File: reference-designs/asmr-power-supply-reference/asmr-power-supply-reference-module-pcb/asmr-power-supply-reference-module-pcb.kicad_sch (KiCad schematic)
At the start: 2 parts

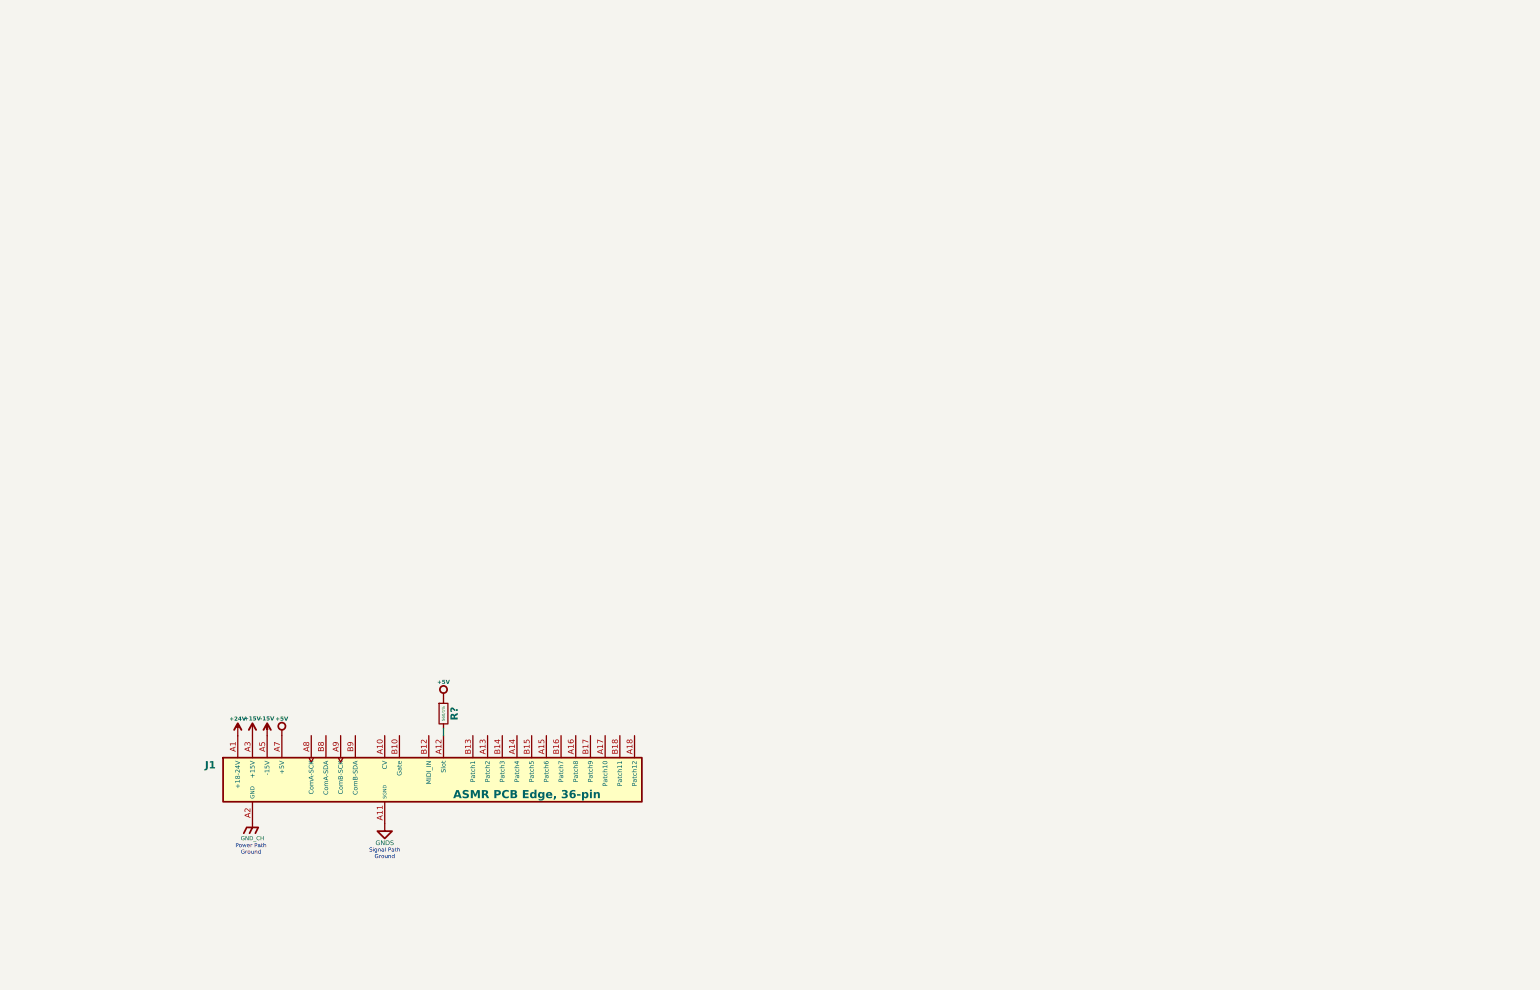
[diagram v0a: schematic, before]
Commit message: First pass on the power supply module.
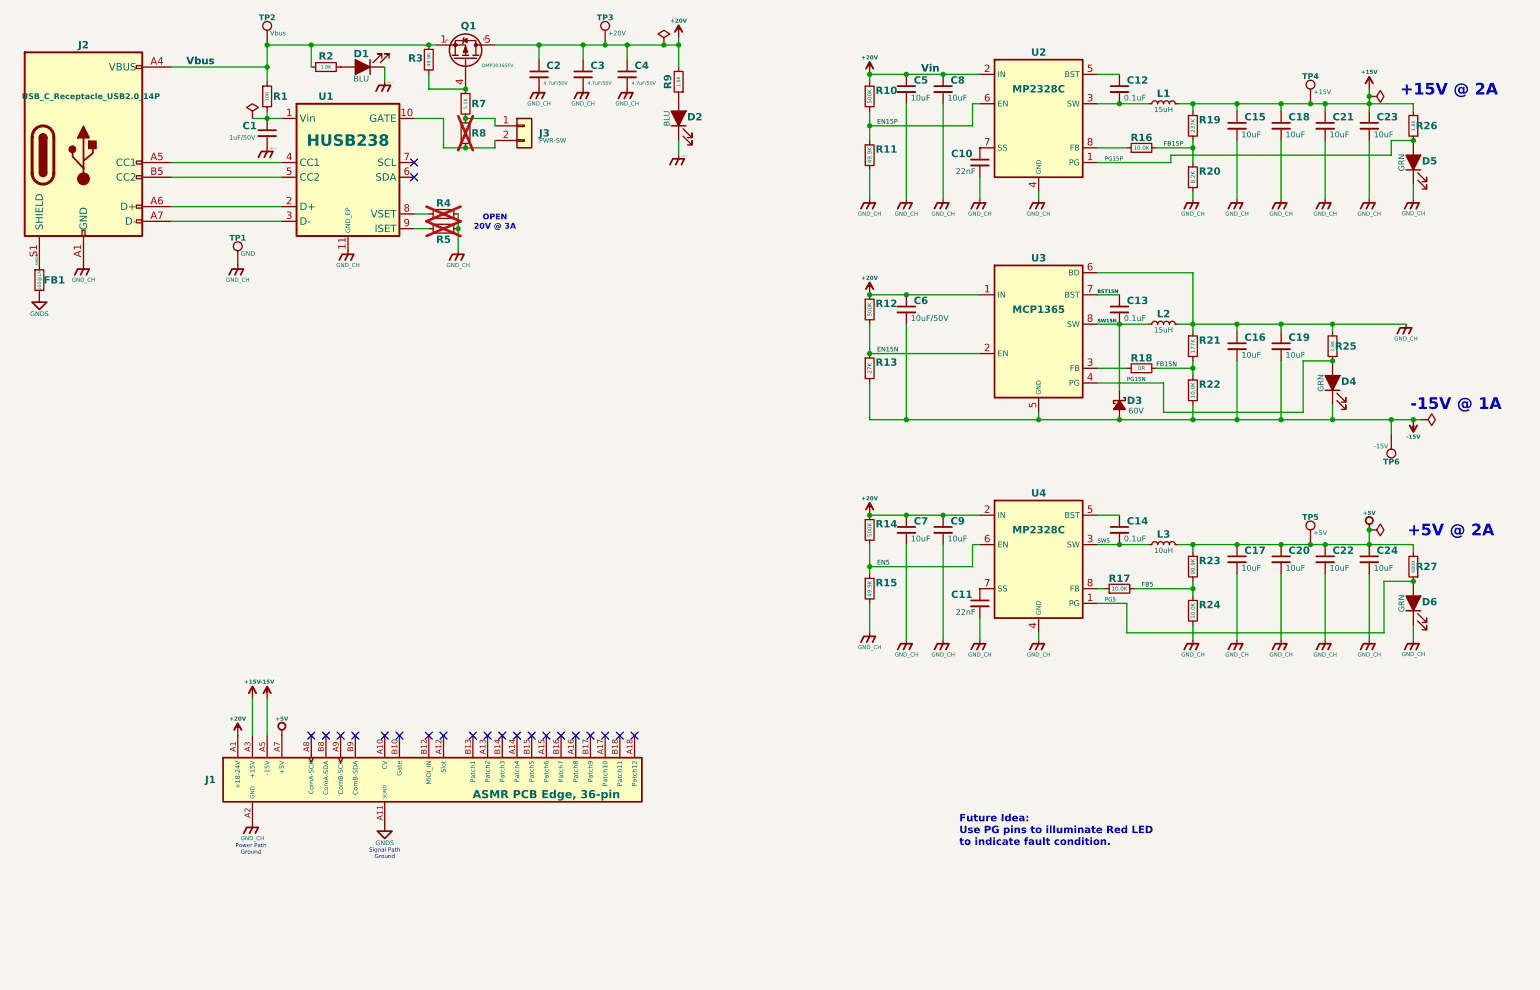
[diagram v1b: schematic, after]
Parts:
- removed R?: 560/1%, symbol CM_Device:R
- added C1: 1uF/50V, CM_Resistor_Capacitor:C_0603_1608Metric, symbol Device:C_Small
- added C10, C11: 22nF, CM_Resistor_Capacitor:C_0603_1608Metric, symbol Device:C_Small
- added C12, C13, C14: 0.1uF, CM_Resistor_Capacitor:C_0603_1608Metric, symbol Device:C_Small
- added C15, C16, C17, C18, C19, C20, C21, C22, C23, C24, C5, C7, C8, C9: 10uF, Capacitor_SMD:C_1206_3216Metric, symbol Device:C_Small
- added C2, C3, C4: 4.7uF/50V, CM_Resistor_Capacitor:C_0603_1608Metric, symbol Device:C_Small
- added C6: 10uF/50V, Capacitor_SMD:C_1206_3216Metric, symbol Device:C_Small
- added D1, D2: BLU, LED_SMD:LED_0603_1608Metric, symbol Device:LED_Filled
- added D3: 60V, Diode_SMD:D_SMF, symbol Device:D_Schottky_Small_Filled
- added D4, D5, D6: GRN, LED_SMD:LED_0603_1608Metric, symbol Device:LED_Filled
- added FB1: 100@1M, CM_Resistor_Capacitor:R_0603_1608Metric, symbol CM_Device:R
- added J2: USB_C_Receptacle_USB2.0_14P, Connector_USB:USB_C_Receptacle_HCTL_HC-TYPE-C-16P-01A, symbol CM_Connector_USB:USB_C_Receptacle_USB2.0_14P
- added J3: PWR-SW, Connector_JST:JST_SH_BM02B-SRSS-TB_1x02-1MP_P1.00mm_Vertical, symbol Connector_Generic:Conn_01x02
- added L1, L2: 15uH, CM_Inductor:SRN5040, symbol Device:L_Small
- added L3: 10uH, CM_Inductor:SRN5040, symbol Device:L_Small
- added Q1: DMP3036SFV, Package_SON:VSON-8_3.3x3.3mm_P0.65mm_NexFET, symbol CM_Transistors_FETs:DMP3036SFV
- added R1: 10R, CM_Resistor_Capacitor:R_0603_1608Metric, symbol CM_Device:R
- added R10, R12, R14: 500K, CM_Resistor_Capacitor:R_0603_1608Metric, symbol Device:R_Small
- added R11, R15: 49.9K, CM_Resistor_Capacitor:R_0603_1608Metric, symbol Device:R_Small
- added R13: 27K, CM_Resistor_Capacitor:R_0603_1608Metric, symbol Device:R_Small
- added R16, R17, R22, R24: 10.0K, CM_Resistor_Capacitor:R_0603_1608Metric, symbol Device:R_Small
- added R18: 0R, CM_Resistor_Capacitor:R_0603_1608Metric, symbol Device:R_Small
- added R19: 237K, CM_Resistor_Capacitor:R_0603_1608Metric, symbol Device:R_Small
- added R2, R25, R26, R9: 1.8K, CM_Resistor_Capacitor:R_0603_1608Metric, symbol CM_Device:R
- added R20: 8.2K, CM_Resistor_Capacitor:R_0603_1608Metric, symbol Device:R_Small
- added R21: 177K, CM_Resistor_Capacitor:R_0603_1608Metric, symbol Device:R_Small
- added R23: 90.9K, CM_Resistor_Capacitor:R_0603_1608Metric, symbol Device:R_Small
- added R27: 680R, CM_Resistor_Capacitor:R_0603_1608Metric, symbol CM_Device:R
- added R3: 49.9K, CM_Resistor_Capacitor:R_0603_1608Metric, symbol CM_Device:R
- added R4, R5: NS, CM_Resistor_Capacitor:R_0603_1608Metric, symbol CM_Device:R
- added R7: 5.1K, CM_Resistor_Capacitor:R_0603_1608Metric, symbol CM_Device:R
- added R8: 0R, CM_Resistor_Capacitor:R_0603_1608Metric, symbol CM_Device:R
- added TP1: GND, TestPoint:TestPoint_Keystone_5015_Micro_Mini, symbol Connector:TestPoint
- added TP2: Vbus, TestPoint:TestPoint_Keystone_5015_Micro_Mini, symbol Connector:TestPoint
- added TP3: +20V, TestPoint:TestPoint_Keystone_5015_Micro_Mini, symbol Connector:TestPoint
- added TP4: +15V, TestPoint:TestPoint_Keystone_5015_Micro_Mini, symbol Connector:TestPoint
- added TP5: +5V, TestPoint:TestPoint_Keystone_5015_Micro_Mini, symbol Connector:TestPoint
- added TP6: -15V, TestPoint:TestPoint_Keystone_5015_Micro_Mini, symbol Connector:TestPoint
- added U1: HUSB238, Package_DFN_QFN:DFN-10-1EP_3x3mm_P0.5mm_EP1.65x2.38mm, symbol CM_Connector_USB:Chip-HUSB238-DFN10
- added U2, U4: MP2328C, Package_TO_SOT_SMD:SOT-583-8, symbol CM_regulator_switching:MP2328C
- added U3: MCP1365, Package_DFN_QFN:DFN-8-1EP_3x3mm_P0.65mm_EP1.55x2.4mm, symbol CM_regulator_switching:MCP1365
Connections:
- net +15V: now also C15.1, C18.1, C21.1, C23.1, L1.2, R19.1, R26.2, TP4.1
- net +5V: now also C17.1, C20.1, C22.1, C24.1, L3.2, R23.1, R27.2, TP5.1
- net -15V: now also C16.2, C19.2, C6.2, D3.2 (A), D4.1 (K), R13.2, R22.2, TP6.1, U3.5 (GND), U3.9 (EP)
- net GNDS: now also FB1.2
- net +24V renamed +18-24V
- net +18-24V: now also C2.1, C3.1, C4.1, C5.1, C6.1, C7.1, C8.1, C9.1, Q1.5 (S), R10.1, R12.1, R14.1, R9.2, TP3.1, U2.2 (IN), U3.1 (IN), U4.2 (IN)
- net GND_CH renamed GND
- net GND: now also C1.2, C10.2, C11.2, C15.2, C16.1, C17.2, C18.2, C19.1, C2.2, C20.2, C21.2, C22.2, C23.2, C24.2, C3.2, C4.2, C5.2, C7.2, C8.2, C9.2, D1.1 (K), D2.1 (K), D5.1 (K), D6.1 (K), J2.A1 (GND), J2.A12 (GND), J2.B1 (GND), J2.B12 (GND), L2.2, R11.2, R15.2, R20.2, R21.1, R24.2, R25.2, R4.2, R5.2, TP1.1, U1.11 (GND_EP), U2.4 (GND), U3.6 (BD), U4.4 (GND)
- new net: J3.1 (Pin_1), R7.2, R8.1
- new net: J3.2 (Pin_2), R8.2, U1.10 (GATE)
- new net: J2.A5 (CC1), U1.4 (CC1)
- new net: J2.A6 (D+), J2.B6 (D+), U1.2 (D+)
- new net: J2.A7 (D-), J2.B7 (D-), U1.3 (D-)
- new net: J2.B5 (CC2), U1.5 (CC2)
- new net: R5.1, U1.9 (ISET)
- new net: R4.1, U1.8 (VSET)
- new net: C10.1, U2.7 (SS)
- new net: D2.2 (A), R9.1
- new net: C12.1, U2.5 (BST)
- new net: C12.2, L1.1, U2.3 (SW)
- new net: R18.1, U3.3 (FB)
- new net: C1.1, R1.2, U1.1 (Vin)
- new net: R16.1, U2.8 (FB)
- new net: C14.1, U4.5 (BST)
- new net: C11.1, U4.7 (SS)
- new net: R17.1, U4.8 (FB)
- new net: D1.2 (A), R2.2
- new net: Q1.4 (G), R3.2, R7.1
- new net BST15N: C13.1, U3.7 (BST)
- new net EN15N: R12.2, R13.1, U3.2 (EN)
- new net EN15P: R10.2, R11.1, U2.6 (EN)
- new net EN5: R14.2, R15.1, U4.6 (EN)
- new net FB15N: R18.2, R21.2, R22.1
- new net FB15P: R16.2, R19.2, R20.1
- new net FB5: R17.2, R23.2, R24.1
- new net PG15N: D4.2 (A), R25.1, U3.4 (PG)
- new net PG15P: D5.2 (A), R26.1, U2.1 (PG)
- new net PG5: D6.2 (A), R27.1, U4.1 (PG)
- new net SHIELD: FB1.1, J2.S1 (SHIELD)
- new net SW15N: C13.2, D3.1 (K), L2.1, U3.8 (SW)
- new net SW5: C14.2, L3.1, U4.3 (SW)
- new net Vbus: J2.A4 (VBUS), J2.A9 (VBUS), J2.B4 (VBUS), J2.B9 (VBUS), Q1.1 (D), Q1.2 (D), Q1.3 (D), R1.1, R2.1, R3.1, TP2.1
- no-connect marks 0 -> 22
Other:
- note added: "+15V @ 2A"
- note added: "+5V @ 2A"
- note added: "-15V @ 1A"
- note added: "Future Idea: Use PG pins to illuminate Red LED to indicate fault condition."
- note added: "OPEN 20V @ 3A"
- title: ASMR - Module PCB Reference Design -> Power Supply Module PCB Reference Design

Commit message: Update design with 64 pin PCI connector.
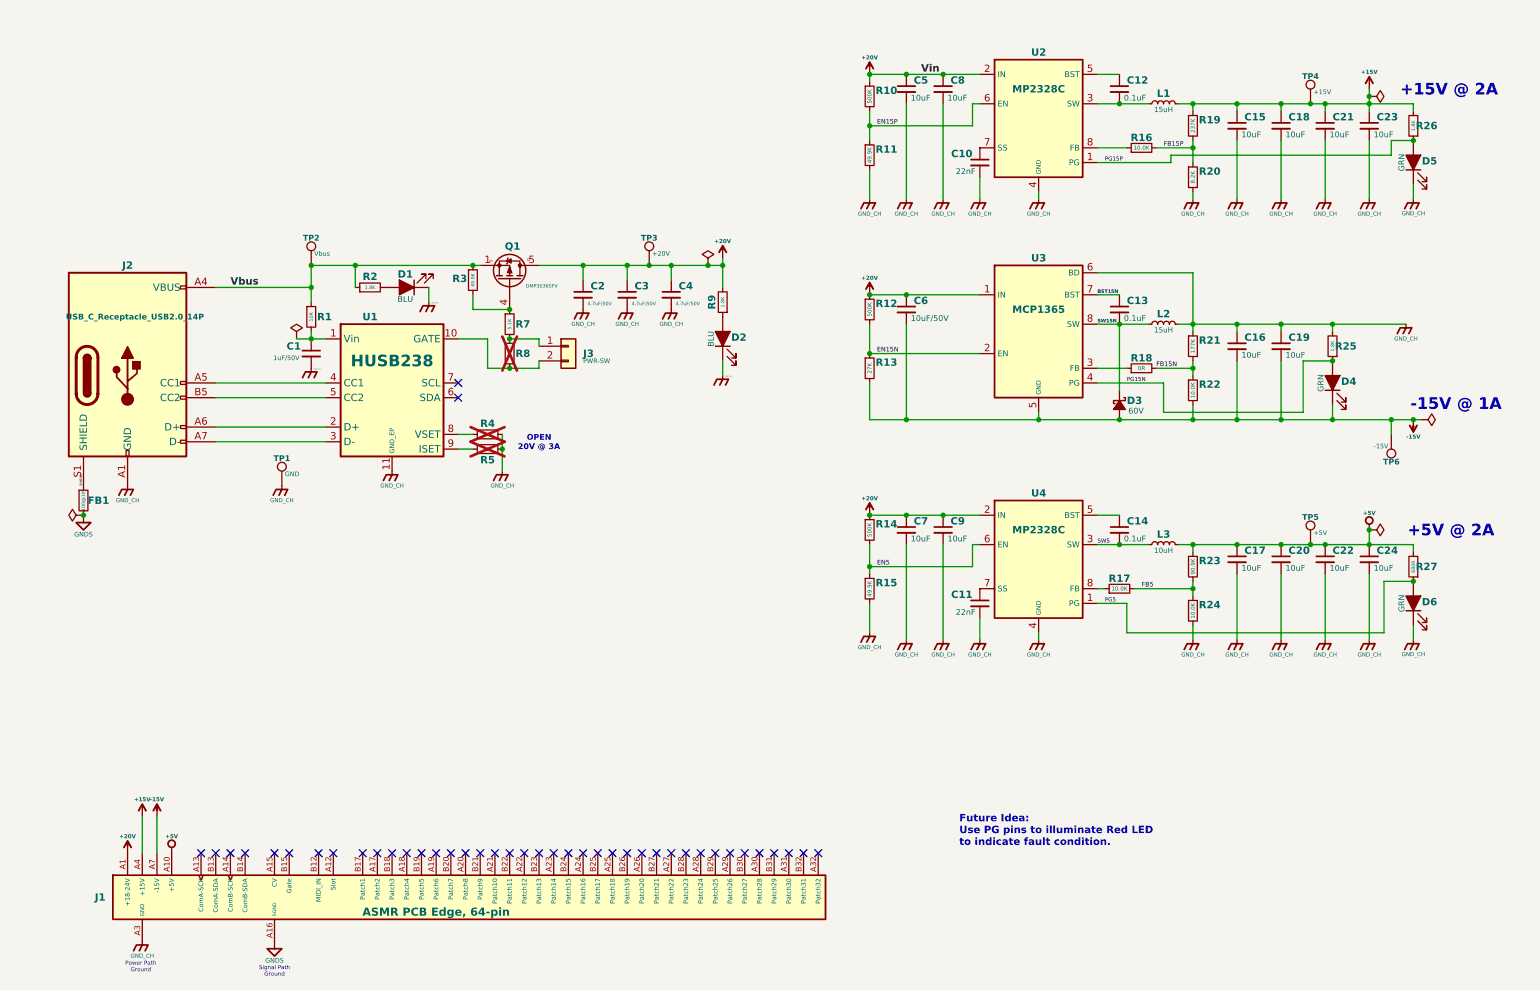
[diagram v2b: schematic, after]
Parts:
- J1: footprint CM_Connector_Edge:ASMR-Edge-36 -> CM_Connector_Edge:ASMR-Edge-64; symbol CM_Connector_Edge:ASMR-36-Edge -> CM_Connector_Edge:ASMR-64-Edge
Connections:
- net +15V: now also J1.A4 (+15V), J1.A5 (+15V), J1.B4 (+15V), J1.B5 (+15V); no longer J1.A3 (+15V), J1.B3 (+15V)
- net +18-24V: now also J1.A2 (+18-24V), J1.B2 (+18-24V)
- net +5V: now also J1.A10 (+5V), J1.A11 (+5V), J1.B10 (+5V), J1.B11 (+5V); no longer J1.A7 (+5V), J1.B7 (+5V)
- net -15V: now also J1.A7 (-15V), J1.A8 (-15V), J1.B7 (-15V), J1.B8 (-15V); no longer J1.A5 (-15V), J1.B5 (-15V)
- net GND: now also J1.A3 (GND), J1.A9 (GND), J1.B3 (GND), J1.B9 (GND); no longer J1.A2 (GND), J1.A4 (GND), J1.B2 (GND), J1.B4 (GND)
- net GNDS: now also J1.A16 (SGND), J1.B16 (SGND); no longer J1.A11 (SGND), J1.B11 (SGND)
- no-connect marks 22 -> 42
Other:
- moved on the sheet: C1, C2, C3, C4, D1, D2, FB1, J2, J3, Q1, R1, R2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

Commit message: More changes to DreamLand.
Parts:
- Q1: footprint Package_SON:VSON-8_3.3x3.3mm_P0.65mm_NexFET -> CM_Chip_Packages:VSON-8_3.3x3.3mm_P0.65mm_NexFET
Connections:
- net +18-24V renamed +20V
- net +20V: now also Q1.6 (S), Q1.7 (S), Q1.8 (S), Q1.PAD (S)
- net GND renamed GND_CH
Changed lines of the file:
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@@
 	(text "Signal Path\nGround"
 		(exclude_from_sim no)
-		(at 58.42 180.848 0)
+		(at 50.8 180.848 0)
 		(effects
 			(font
@@
 	)
 	(no_connect
-		(at 50.8 161.29)
+		(at 55.88 161.29)
 	)
 	(no_connect
@@
 		)
 	)
-	(label "Vin"
-		(at 170.18 26.67 0)
-		(effects
-			(font
-				(size 1.27 1.27)
-				(thickness 0.254)
-				(bold yes)
-			)
-			(justify left bottom)
-		)
-	)
 	(label "FB15P"
 		(at 212.09 39.37 0)
@@
 	(symbol
 		(lib_id "CM_power:GNDS")
-		(at 58.42 176.53 0)
+		(at 50.8 176.53 0)
 		(unit 1)
 		(exclude_from_sim no)
@@
 		(dnp no)
 		(property "Reference" "#PWR012"
-			(at 58.42 182.88 0)
+			(at 50.8 182.88 0)
 			(effects
 				(font
@@
 		)
 		(property "Value" "GNDS"
-			(at 58.42 179.832 0)
+			(at 50.8 179.832 0)
 			(effects
 				(font
@@
 		)
 		(property "Footprint" ""
-			(at 58.42 176.53 0)
+			(at 50.8 176.53 0)
 			(effects
 				(font
@@
 		)
 		(property "Datasheet" ""
-			(at 58.42 176.53 0)
+			(at 50.8 176.53 0)
 			(effects
 				(font
@@
 		)
 		(property "Description" "Power symbol creates a global label with name \"GNDS\" , signal ground"
-			(at 58.42 176.53 0)
+			(at 50.8 176.53 0)
 			(effects
 				(font
@@
 		(dnp no)
 		(property "Reference" "Q1"
-			(at 99.568 56.388 90)
+			(at 99.06 56.642 90)
 			(do_not_autoplace yes)
 			(effects
@@
 		)
 		(property "Value" "DMP3036SFV"
-			(at 101.854 63.246 90)
+			(at 100.838 63.246 90)
 			(do_not_autoplace yes)
 			(effects
 				(font
-					(size 0.6 0.6)
+					(size 0.8 0.8)
 				)
 				(justify left)
 			)
 		)
-		(property "Footprint" "Package_SON:VSON-8_3.3x3.3mm_P0.65mm_NexFET"
+		(property "Footprint" "CM_Chip_Packages:VSON-8_3.3x3.3mm_P0.65mm_NexFET"
 			(at 94.361 31.877 0)
 			(effects
@@
 		(pin "5"
 		)
+		(pin "6"
+		)
+		(pin "7"
+		)
+		(pin "8"
+		)
+		(pin "PAD"
+		)
 		(instances

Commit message: Tune final power supply design.
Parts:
- J3: footprint Connector_JST:JST_SH_BM02B-SRSS-TB_1x02-1MP_P1.00mm_Vertical -> CM_Connector_JST:JST_SH_BM02B-SRSS-TB_1x02-1MP_P1.00mm_Vertical
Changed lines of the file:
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@@
 			)
 		)
-		(property "Footprint" "Connector_JST:JST_SH_BM02B-SRSS-TB_1x02-1MP_P1.00mm_Vertical"
+		(property "Footprint" "CM_Connector_JST:JST_SH_BM02B-SRSS-TB_1x02-1MP_P1.00mm_Vertical"
 			(at 109.22 73.66 0)
 			(effects

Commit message: Rev.B Notes and changes. Work in Progress.
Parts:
- added C25: 0.1uF, CM_Resistor_Capacitor:C_0603_1608Metric, symbol Device:C_Small
- added D7: 11.5V, Diode_SMD:D_SOD-323_HandSoldering, symbol Device:D_Zener_Small_Filled
- R10, R14: value 500K -> 499K
- R12: value 500K -> 10K
- R13: value 27K -> NS; now not fitted; now left out of the parts list
- R21: value 177K -> 174K
- R25, R26: value 1.8K -> 680R
- R27: value 680R -> 220R
- U3: value MCP1365 -> MCP16365; MPN MCP1365 -> MCP16365
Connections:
- net -15V: now also C25.2
- net GND_CH: now also D7.1 (K); no longer U3.6 (BD)
- new net: C25.1, D7.2 (A), U3.6 (BD)
- no-connect marks 42 -> 44
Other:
- note added: "Change C2,C3,C4 to 0805."
- moved on the sheet: C16, C19, C6, D4, R25
